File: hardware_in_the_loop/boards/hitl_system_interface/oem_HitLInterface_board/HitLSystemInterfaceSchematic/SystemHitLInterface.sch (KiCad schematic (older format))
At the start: 50 parts, among them J1 CONN_02X03, J2 Conn_01x04_Female, J3 Conn_01x04_Female, J4 Barrel_Jack, J5 Conn_01x04_Female, J6 Conn_01x01_Female, J7 Conn_01x01_Female, J8 Conn_01x01_Female, U1 ATmega328P-AU, U101 TPS560430YF, U3 USB_MicroB, U4 FT232RL, U6 NanoFit_RA_TH_12, Y1 Crystal_SMD

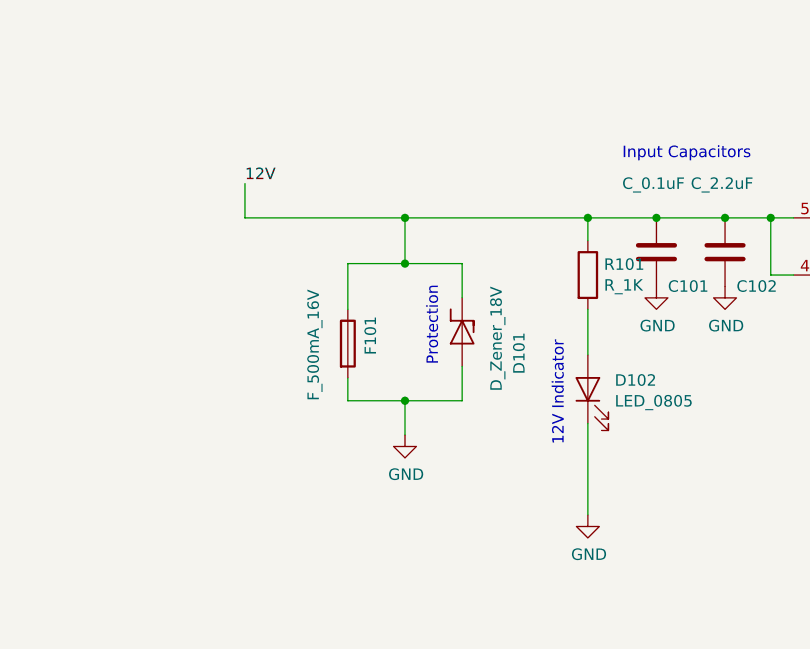
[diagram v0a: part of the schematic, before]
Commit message: Updated Fuse and Zener Diode on Buck Converter
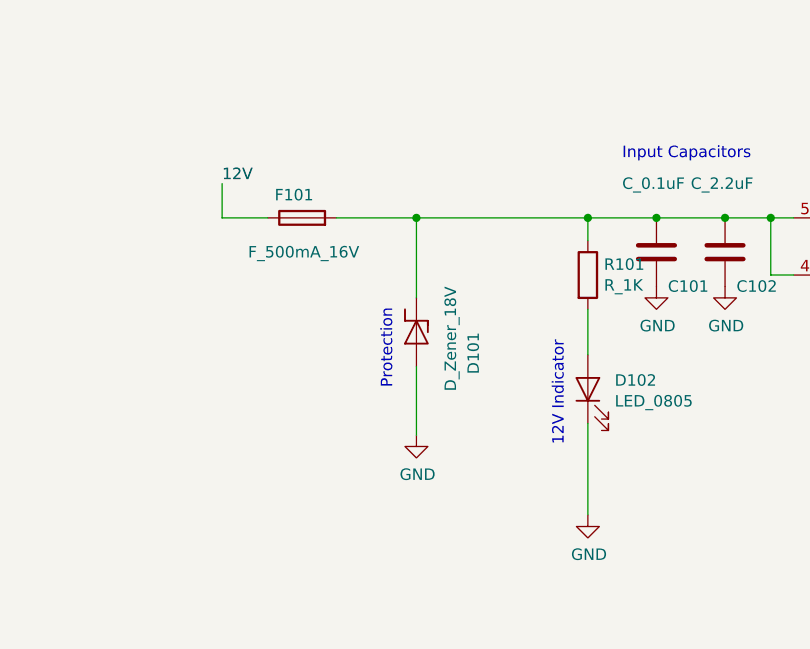
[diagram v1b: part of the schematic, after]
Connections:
- net 12V: no longer C101.1, C102.1, D101.1 (K), R101.1, U101.4 (EN), U101.5 (VIN)
- net GND: no longer F101.2
- new net: C101.1, C102.1, D101.1 (K), F101.2, R101.1, U101.4 (EN), U101.5 (VIN)
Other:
- moved on the sheet: D101, F101
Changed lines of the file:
@@
 Text Notes 8150 7550 1    50   ~ 0
 12V Indicator
-Text Notes 7600 7200 1    50   ~ 0
+Text Notes 7400 7300 1    50   ~ 0
 Protection
 $Comp
 L power:GND #PWR014
 U 1 1 5FCD86BF
-P 7450 7500
-F 0 "#PWR014" H 7450 7250 50  0001 C CNN
-F 1 "GND" H 7455 7327 50  0000 C CNN
-F 2 "" H 7450 7500 50  0001 C CNN
-F 3 "" H 7450 7500 50  0001 C CNN
-	1    7450 7500
+P 7500 7500
+F 0 "#PWR014" H 7500 7250 50  0001 C CNN
+F 1 "GND" H 7505 7327 50  0000 C CNN
+F 2 "" H 7500 7500 50  0001 C CNN
+F 3 "" H 7500 7500 50  0001 C CNN
+	1    7500 7500
 	1    0    0    -1
 $EndComp
@@
 L formula:F_500mA_16V F101
 U 1 1 5FCD25BC
-P 7200 7100
-F 0 "F101" V 7300 7050 50  0000 L CNN
-F 1 "F_500mA_16V" V 7050 6850 50  0000 L CNN
-F 2 "footprints:Fuse_1210" V 7130 7100 50  0001 C CNN
-F 3 "https://belfuse.com/resources/CircuitProtection/datasheets/0ZCH%20Nov2016.pdf" V 7280 7100 50  0001 C CNN
-F 4 "DK" H 7200 7100 60  0001 C CNN "MFN"
-F 5 "507-1786-1-ND" H 7200 7100 60  0001 C CNN "MPN"
-F 6 "https://www.digikey.com/product-detail/en/bel-fuse-inc/0ZCH0050FF2G/507-1786-1-ND/4156209" V 7680 7500 60  0001 C CNN "PurchasingLink"
-	1    7200 7100
-	1    0    0    -1
-$EndComp
-Wire Wire Line
-	7450 7350 7450 7500
+P 7000 6550
+F 0 "F101" V 7100 6500 50  0000 L CNN
+F 1 "F_500mA_16V" V 6850 6300 50  0000 L CNN
+F 2 "footprints:Fuse_1210" V 6930 6550 50  0001 C CNN
+F 3 "https://belfuse.com/resources/CircuitProtection/datasheets/0ZCH%20Nov2016.pdf" V 7080 6550 50  0001 C CNN
+F 4 "DK" H 7000 6550 60  0001 C CNN "MFN"
+F 5 "507-1786-1-ND" H 7000 6550 60  0001 C CNN "MPN"
+F 6 "https://www.digikey.com/product-detail/en/bel-fuse-inc/0ZCH0050FF2G/507-1786-1-ND/4156209" V 7480 6950 60  0001 C CNN "PurchasingLink"
+	1    7000 6550
+	0    -1   -1   0
+$EndComp
 $Comp
 L formula:D_Zener_18V D101
 U 1 1 5FCCB5C8
-P 7700 7050
-F 0 "D101" H 7700 7300 50  0000 L CNN
-F 1 "D_Zener_18V" H 7500 7200 50  0000 L CNN
-F 2 "footprints:DO-214AA" H 7600 7050 50  0001 C CNN
-F 3 "http://www.mccsemi.com/up_pdf/SMBJ5338B-SMBJ5388B(SMB).pdf" H 7700 7150 50  0001 C CNN
-F 4 "DK" H 7900 7350 60  0001 C CNN "MFN"
-F 5 "SMBJ5355B-TPMSCT-ND" H 7800 7250 60  0001 C CNN "MPN"
-F 6 "https://www.digikey.com/products/en?keywords=SMBJ5355B-TPMSCT-ND" H 8100 7550 60  0001 C CNN "PurchasingLink"
-	1    7700 7050
+P 7500 7050
+F 0 "D101" H 7500 7300 50  0000 L CNN
+F 1 "D_Zener_18V" H 7300 7200 50  0000 L CNN
+F 2 "footprints:DO-214AA" H 7400 7050 50  0001 C CNN
+F 3 "http://www.mccsemi.com/up_pdf/SMBJ5338B-SMBJ5388B(SMB).pdf" H 7500 7150 50  0001 C CNN
+F 4 "DK" H 7700 7350 60  0001 C CNN "MFN"
+F 5 "SMBJ5355B-TPMSCT-ND" H 7600 7250 60  0001 C CNN "MPN"
+F 6 "https://www.digikey.com/products/en?keywords=SMBJ5355B-TPMSCT-ND" H 7900 7550 60  0001 C CNN "PurchasingLink"
+	1    7500 7050
 	0    1    1    0
 $EndComp
@@
 	3850 3900 4000 3900
 Wire Wire Line
-	7200 6950 7200 6750
-Wire Wire Line
-	7200 6750 7450 6750
-Wire Wire Line
-	7700 6750 7700 6900
-Wire Wire Line
-	7200 7250 7200 7350
-Wire Wire Line
-	7200 7350 7450 7350
-Wire Wire Line
-	7700 7350 7700 7200
-Connection ~ 7450 7350
-Wire Wire Line
-	7450 7350 7700 7350
-Wire Wire Line
-	7450 6750 7450 6550
-Connection ~ 7450 6750
-Wire Wire Line
-	7450 6750 7700 6750
-Wire Wire Line
-	8250 6550 7450 6550
-Wire Wire Line
-	6750 6400 6750 6550
-Connection ~ 8250 6550
-Connection ~ 7450 6550
-Wire Wire Line
-	7450 6550 6750 6550
-Text Label 6750 6400 0    50   ~ 0
+	6650 6400 6650 6550
+Text Label 6650 6400 0    50   ~ 0
 12V
 $Comp
@@
 	1    0    0    -1
 $EndComp
+Connection ~ 8250 6550
+Wire Wire Line
+	7150 6550 7500 6550
+Wire Wire Line
+	6850 6550 6650 6550
+Wire Wire Line
+	7500 6900 7500 6550
+Connection ~ 7500 6550
+Wire Wire Line
+	7500 6550 8250 6550
+Wire Wire Line
+	7500 7200 7500 7500
 $EndSCHEMATC
